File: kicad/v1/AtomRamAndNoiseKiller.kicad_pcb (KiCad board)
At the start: 2 copper layers, 76.8 x 49.5 mm, 21 parts, among them J1 Conn_02x10_Counter_Clockwise, J2 Conn_01x02, J3 Conn_01x02, J4 Conn_01x09, J5 Conn_01x09, J6 Conn_01x03, U1 74LS123, U2 74LS00, U3 74LS245, U4 74LS573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

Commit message: KiCad: Fully routed
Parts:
- added J7: Conn_01x01, Connector_PinHeader_2.54mm:PinHeader_1x01_P2.54mm_Horizontal, F.Cu at (204.5, 149.2)
- C1, C2, C3, C4, C5: footprint Capacitor_THT:C_Rect_L7.0mm_W2.0mm_P5.00mm -> Capacitor_THT:C_Axial_L3.8mm_D2.6mm_P7.50mm_Horizontal
- J1: value Conn_02x10_Counter_Clockwise -> Conn_01x10; footprint Package_DIP:DIP-20_W7.62mm_Socket -> footprints:FinePinHeader_1x10_P2.54mm_Vertical
- J2: value Conn_01x02 -> Conn_01x10; footprint Connector_PinHeader_2.54mm:PinHeader_1x02_P2.54mm_Vertical -> footprints:FinePinHeader_1x10_P2.54mm_Vertical; moved to B.Cu
- J4, J5: footprint Connector_PinHeader_2.54mm:PinHeader_1x09_P2.54mm_Vertical -> footprints:FinePinHeader_1x09_P2.54mm_Vertical; moved to B.Cu
- J6: footprint Connector_PinHeader_2.54mm:PinHeader_1x03_P2.54mm_Vertical -> footprints:FinePinHeader_1x03_P2.54mm_Vertical; moved to B.Cu
- moved J2 83.7 mm to (153.0, 110.5), turned to 180 degrees
- moved C7 59.6 mm to (165.1, 140.3)
- moved C6 47.3 mm to (207.0, 117.5), turned to 270 degrees
- moved R3 43.1 mm to (152.4, 137.2)
- moved J3 33.7 mm to (167.6, 137.2), turned to 90 degrees
- moved R1 24.3 mm to (152.4, 140.3)
- moved R2 21.0 mm to (204.5, 146.1), turned to 90 degrees
- moved C4 6.35 mm to (177.2, 107.3), turned to 180 degrees
- moved C5 2.84 mm to (189.2, 111.8)
- moved C1 1.27 mm to (158.1, 144.1)
- moved C2 1.27 mm to (182.2, 144.1)
- moved C3 1.27 mm to (163.2, 107.3)
- turned J4 to 180 degrees
- turned J5 to 180 degrees
- turned J6 to 180 degrees
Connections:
- J2 pad 1: /RRDISABLE -> /PD0
- J2 pad 2: /RRDISABLE -> /PD1
- U5 pad 1: (no net) -> GND
- U5 pad 10: /A0 -> /A2
- U5 pad 11: /RD0 -> /RD5
- U5 pad 12: /RD1 -> /RD6
- U5 pad 13: /RD2 -> /RD7
- U5 pad 15: /RD3 -> /RD4
- U5 pad 16: /RD4 -> /RD3
- U5 pad 17: /RD5 -> /RD2
- U5 pad 18: /RD6 -> /RD1
- U5 pad 19: /RD7 -> /RD0
- U5 pad 2: /A12 -> /A10
- U5 pad 21: /A10 -> /A6
- U5 pad 23: /A11 -> /A9
- U5 pad 24: /A9 -> /A8
- U5 pad 25: /A8 -> /A7
- U5 pad 26: (no net) -> GND
- U5 pad 3: /A7 -> /A11
- U5 pad 4: /A6 -> /A12
- U5 pad 8: /A2 -> /A0
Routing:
- net /NVDG: track 0.00 -> 91.9 mm
- net /A10: track 0.00 -> 65.5 mm, vias 0 -> 2
- net /A12: track 0.00 -> 65.2 mm, vias 0 -> 2
- net /A11: track 0.00 -> 65.0 mm, vias 0 -> 2
- net /NWE: track 0.00 -> 51.1 mm
- net /RD4: track 7.40 -> 45.9 mm
- net /RD1: track 7.40 -> 45.9 mm
- net /RD0: track 7.40 -> 45.9 mm
- net /RD3: track 7.40 -> 45.9 mm
- net /RD2: track 7.40 -> 45.9 mm
- net Net-(J3-Pad2): track 0.00 -> 33.4 mm
- net Net-(U1-Pad4): track 0.00 -> 29.1 mm
- net /A9: track 0.00 -> 28.8 mm
- net /A5: track 0.00 -> 28.8 mm
- net /A0: track 0.00 -> 28.8 mm
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- added copper zone on B.Cu, net VCC
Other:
- board size 76.8 x 49.5 mm -> 70.5 x 49.5 mm
- board text added: "8K x 8 SRAM"
- board text added: "Atom Noise Killer (c) 2019 Hoglet"
- board text added: "RAMROM disable"
- board text added: "enable"
- board text added: "fit in IC29"
- board text added: "fit in IC30"
- board text added: "fit in IC33"

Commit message: More work
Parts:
- added J8: Conn_01x01, Connector_PinHeader_2.54mm:PinHeader_1x01_P2.54mm_Horizontal, F.Cu at (204.5, 149.2)
- J3: value Conn_01x02 -> Conn_01x03; footprint Connector_PinHeader_2.54mm:PinHeader_1x02_P2.54mm_Vertical -> footprints:FinePinHeader_1x03_P2.54mm_Vertical; moved to B.Cu
- J7: value Conn_01x01 -> Conn_01x02; footprint Connector_PinHeader_2.54mm:PinHeader_1x01_P2.54mm_Horizontal -> Connector_PinHeader_2.54mm:PinHeader_1x02_P2.54mm_Vertical
- moved J3 55.7 mm to (216.5, 110.5), turned to 180 degrees
- moved J7 38.8 mm to (167.6, 137.2), turned to 90 degrees
- moved C6 9.57 mm to (205.7, 108.0)
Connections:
- J3 pad 1: /LOAD -> Net-(J3-Pad1)
- J5 pad 9: /NWE -> Net-(J5-Pad9)
- J7 pad 1: /RRDISABLE -> /LOAD
- U2 pad 8: Net-(J3-Pad2) -> Net-(J7-Pad2)
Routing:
- net Net-(J7-Pad2): track 0.00 -> 33.4 mm
- net Net-(J3-Pad2): track 33.4 -> 0.00 mm
- net /NWE: track 51.1 -> 18.0 mm
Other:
- outline, holes or cut-outs redrawn
- board text added: "Atom 8K Ram and Noise Killer (c) 2019 Hoglet"
- board text added: "Disable from RAMROM"
- board text added: "Enable"
- board text added: "Fit in IC29"
- board text added: "Fit in IC30"
- board text added: "Fit in IC32"
- board text added: "Fit in IC33"
- board text removed: "Atom Noise Killer (c) 2019 Hoglet"
- board text removed: "RAMROM disable"
- board text removed: "enable"
- board text removed: "fit in IC29"
- board text removed: "fit in IC30"
- board text removed: "fit in IC33"

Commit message: Almost finished
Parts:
- R2: value 47K -> 10K
- R3: value 10K -> 47K
- moved R2 52.8 mm to (152.4, 137.2), turned to 0 degrees
- moved R3 52.8 mm to (204.5, 146.1), turned to 90 degrees
- moved J3 5.08 mm to (221.6, 110.5)
- moved J4 5.08 mm to (214.0, 128.3)
- moved J5 5.08 mm to (221.6, 128.3)
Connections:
- R2 pad 1: /RRDISABLE -> VCC
- R2 pad 2: GND -> /LOAD
- R3 pad 1: VCC -> /RRDISABLE
- R3 pad 2: /LOAD -> GND
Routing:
- net /A9: track 28.8 -> 35.4 mm
- net /A8: track 26.7 -> 32.5 mm
- net /NWE: track 18.0 -> 23.1 mm
- net /A5: track 28.8 -> 33.8 mm
- net /A4: track 28.8 -> 33.8 mm
- net /A3: track 28.8 -> 33.8 mm
- net /A2: track 28.8 -> 33.8 mm
- net /A0: track 28.8 -> 33.8 mm
- net /A1: track 28.8 -> 33.8 mm
- net /A6: track 10.2 -> 14.4 mm
- net /A7: track 26.7 -> 30.6 mm
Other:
- board size 70.5 x 49.5 mm -> 76.2 x 49.5 mm
- board text added: "'00"
- board text added: "'123"
- board text added: "'245"
- board text added: "'573"
- board text added: "Acorn Atom 8K Video RAM and Noise-Killer (c) 2019 Hoglet"
- board text added: "Fit in IC36"
- board text added: "Fit in IC37"
- board text added: "also compatible with 32K x 8 SRAM"
- board text removed: "Atom 8K Ram and Noise Killer (c) 2019 Hoglet"
- board text removed: "Fit in IC32"
- board text removed: "Fit in IC33"

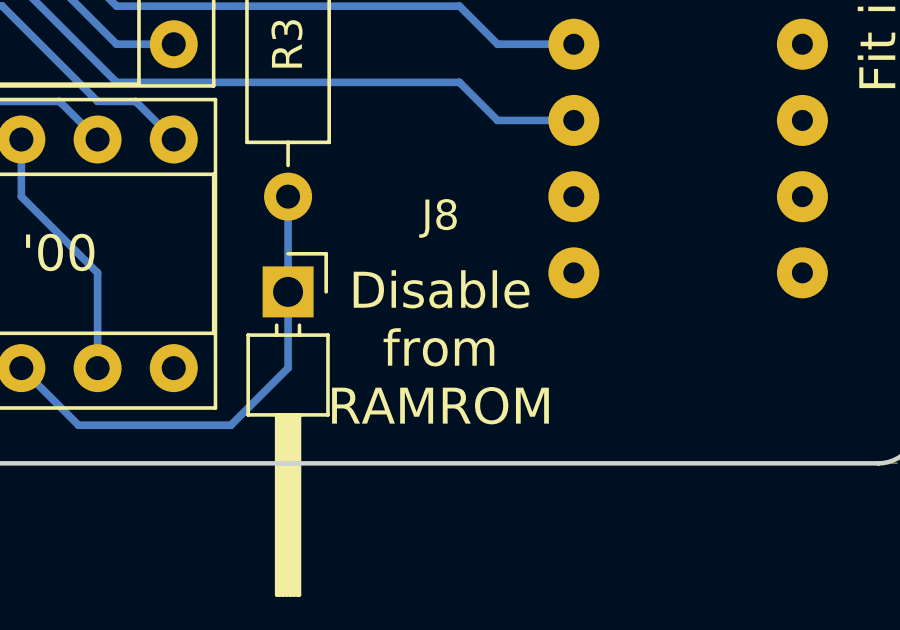
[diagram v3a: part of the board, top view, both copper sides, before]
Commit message: Switched to HCT parts (cheaper)
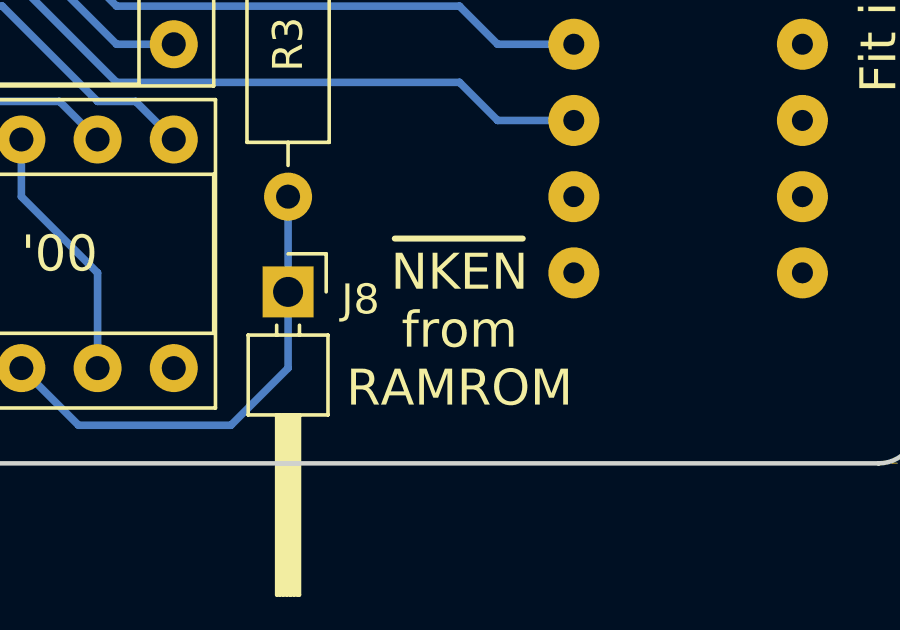
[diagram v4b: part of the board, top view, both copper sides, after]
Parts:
- C7: value 150p -> 68p
- R3: value 47K -> 4K7
- U1: value 74LS123 -> 74HCT123
- U2: value 74LS00 -> 74HCT00
- U3: value 74LS245 -> 74HCT245
- U4: value 74LS573 -> 74HCT573
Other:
- board text added: "NKEN from RAMROM"
- board text removed: "Disable from RAMROM"
